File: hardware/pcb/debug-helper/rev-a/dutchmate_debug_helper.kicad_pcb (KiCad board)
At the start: 4 copper layers, 21 x 64.9 mm, 42 parts, among them J1 Conn_02x08_Odd_Even, U1 SN74LV4T125, U2 TXU0202DCUR, U4 TPD6E05U06RVZ, U5 TXU0104PWR, U6 TPD4E05U06DQA, U7 SN74LVC2G06DBV, U8 SN74LVC2G06DBV

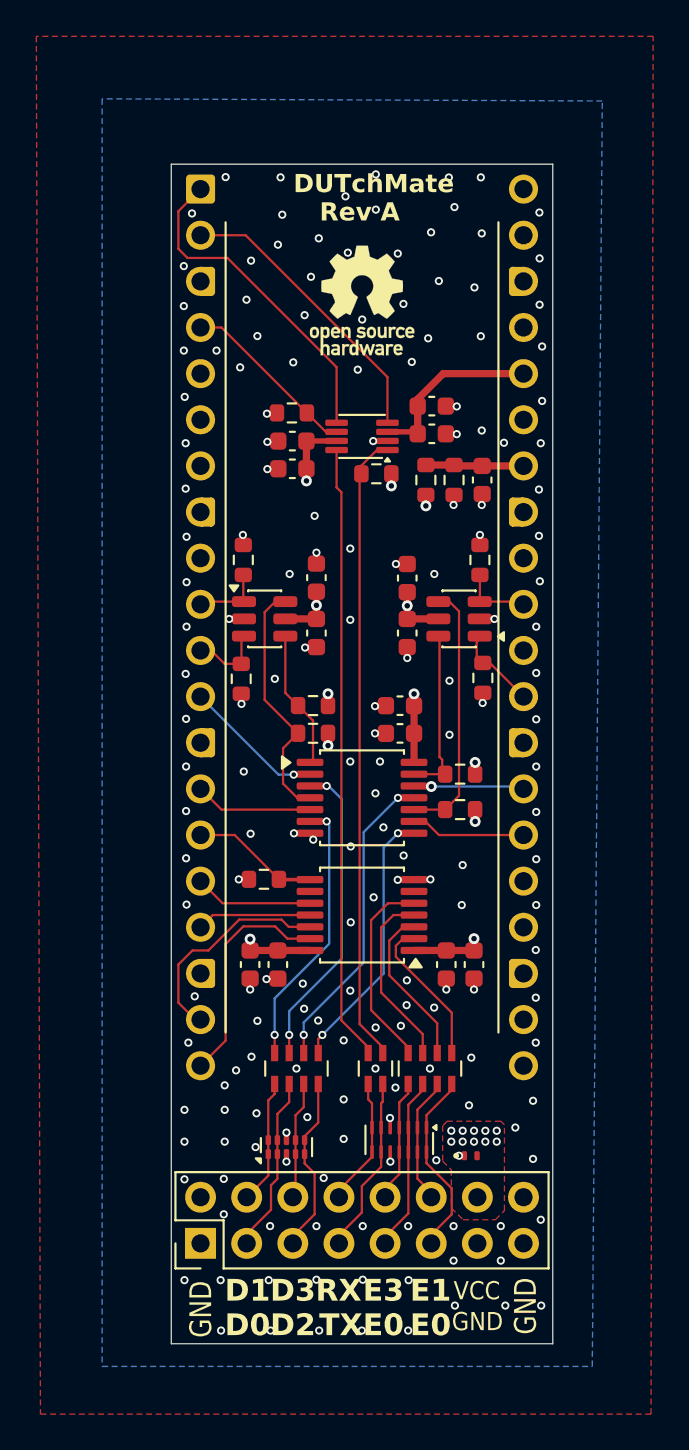
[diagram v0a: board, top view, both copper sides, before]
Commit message: Finalize Rev-A KiCad source corrections
Signed-off-by: Nahit Pawar <nahitpawar@gmail.com>
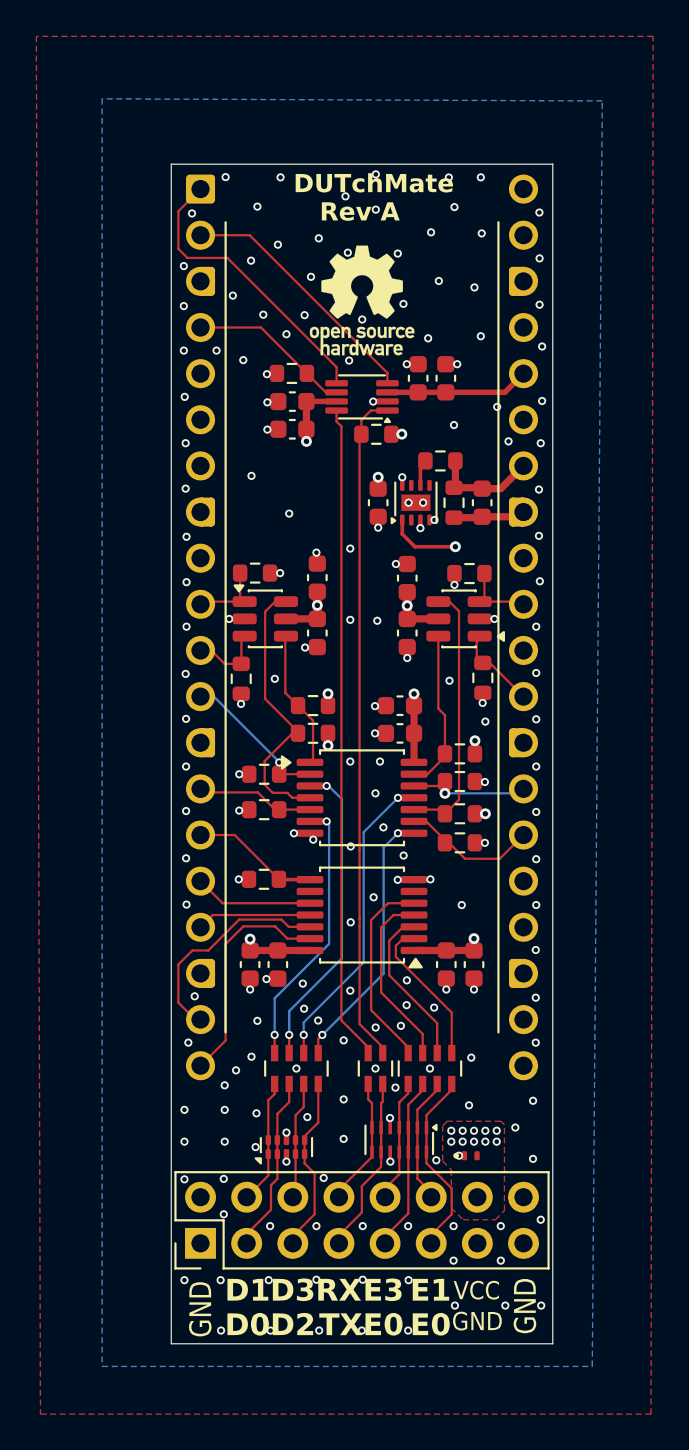
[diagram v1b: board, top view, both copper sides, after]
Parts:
- added C16: 100nF, Capacitor_SMD:C_0603_1608Metric, F.Cu at (130.7, 92.1)
- added R14: 10K, Resistor_SMD:R_0603_1608Metric, F.Cu at (124.4, 107.1)
- added R15: 10K, Resistor_SMD:R_0603_1608Metric, F.Cu at (124.4, 109.0)
- added R16: 10K, Resistor_SMD:R_0603_1608Metric, F.Cu at (135.2, 110.8)
- added R17: 10K, Resistor_SMD:R_0603_1608Metric, F.Cu at (135.2, 107.5)
- added U3: TMUX2819DSGR, Package_SON:Texas_DSG0008A_WSON-8-1EP_2x2mm_P0.5mm_EP0.9x1.6mm, F.Cu at (132.7, 92.1)
- A1: value RaspberryPi_Pico -> Raspberry Pi Pico 2
- R1, R2, R3, R4: value 100K -> 4.7K
- R12, R5: value 10K -> 4.7K
- R13: value 47K -> 10K
- R6, R7, R8, R9: value 47K -> 4.7K
- RN3, RN4: value 181R -> 180R
- moved C2 3.15 mm to (134.4, 85.3), turned to 90 degrees
- moved R12 2.18 mm to (125.9, 85.0)
- moved C1 2.17 mm to (125.9, 86.6)
- moved C11 2.17 mm to (125.9, 88.1)
- moved R13 2.17 mm to (130.6, 88.4)
- moved U2 2.17 mm to (129.8, 86.3)
- moved C12 1.71 mm to (132.8, 85.3), turned to 90 degrees
- moved R10 1.32 mm to (134.1, 89.8), turned to 0 degrees
- moved C7 1.25 mm to (136.4, 92.1)
- moved R11 1.25 mm to (134.8, 92.1)
- moved R8 1.12 mm to (135.2, 106.0)
- moved R1 0.97 mm to (123.9, 96.0), turned to 0 degrees
- moved R4 0.95 mm to (135.7, 96.0), turned to 180 degrees
- moved R9 0.23 mm to (135.2, 109.2)
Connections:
- net Net-(U7-1Y) renamed /DBG_CTRL_OE1_N
- net Net-(U7-2Y) renamed /DBG_CTRL_OE0_N
- net Net-(U8-1Y) renamed /DBG_CTRL_OE3_N
- net Net-(U8-2Y) renamed /DBG_CTRL_OE2_N
- A1 pad 33: GND -> GNDA
- C7 pad 2: GND -> GNDA
- R10 pad 1: DUT_VIO -> Net-(U3-D)
- R11 pad 2: GND -> GNDA
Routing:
- net GNDA: track 0.00 -> 3.51 mm
- net DUT_VIO: track 13.6 -> 16.9 mm
- net Net-(RN5B-R2.1): track 33.6 -> 35.8 mm
- net /DBG_UART_TX: track 18.3 -> 16.1 mm
- net /DBG_UART_RX: track 16.0 -> 14.0 mm
- net +3.3V: track 19.6 -> 17.6 mm, vias 3 -> 6
- net Net-(RN5A-R1.1): track 34.8 -> 36.6 mm
- net /DBG_CTRL_OE1_N: track 13.2 -> 14.4 mm
- net Net-(U3-D): track 0.00 -> 1.08 mm
- net /DBG_CTRL_DATA2: track 5.72 -> 6.67 mm
- net /DBG_UART_IF_EN: track 9.87 -> 8.97 mm
- net GND: vias 184 -> 187
